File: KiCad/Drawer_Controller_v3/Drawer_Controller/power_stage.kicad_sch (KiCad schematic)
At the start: 27 parts, among them U10 AMS1117-3.3, U9 TPS54331DR

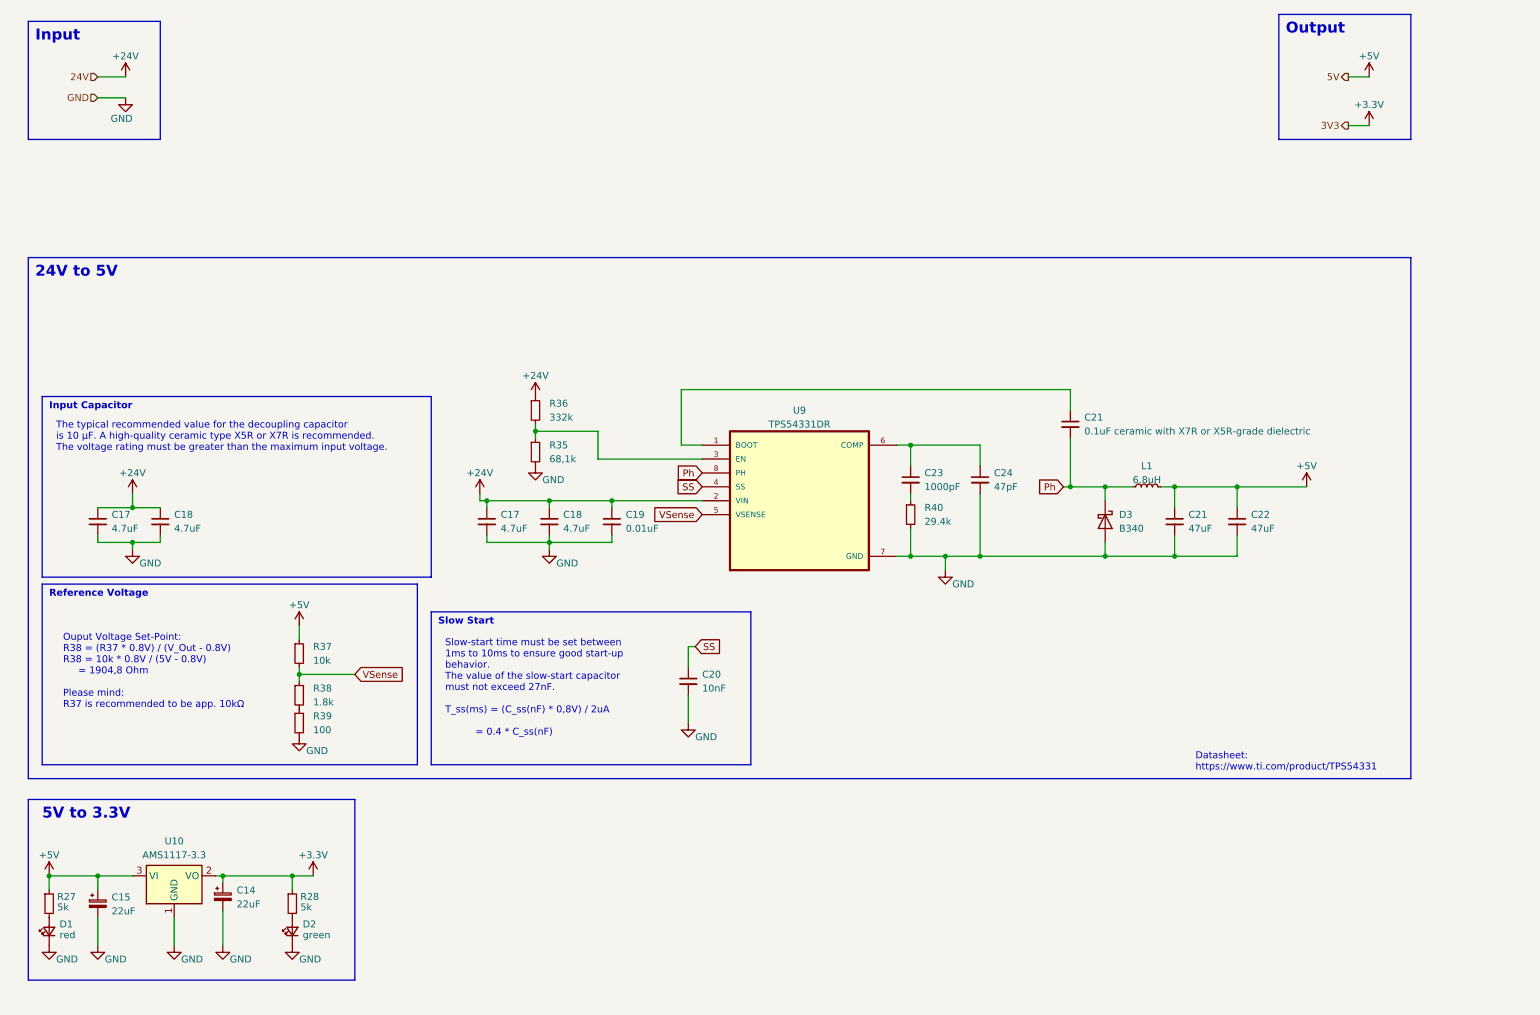
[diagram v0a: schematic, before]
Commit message: Further progress with the power stage including lots of documentation
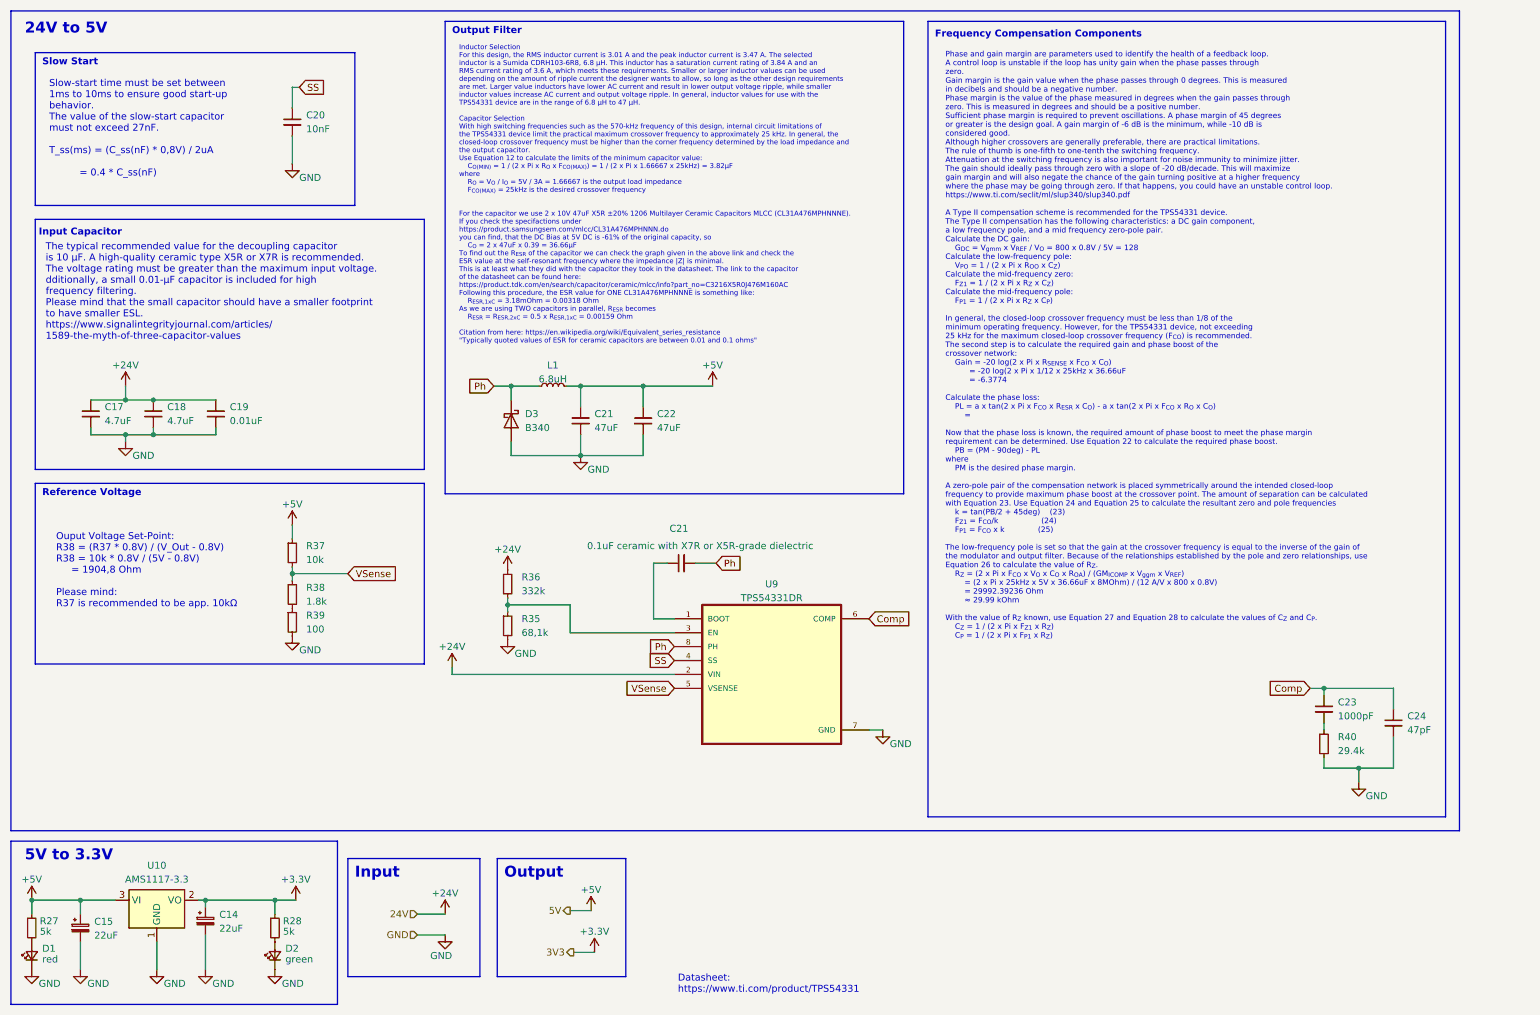
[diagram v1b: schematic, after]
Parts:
- removed C17 (x2), C18 (x2): 4.7uF, symbol Device:C_Small
- added C17, C18: 4.7uF, symbol Device:C_Small
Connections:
- net +24V: now also C17.1, C18.1
- net GND: now also C17.2, C18.2
- net Comp: now reaches C23.1, C24.1, U9.6 (COMP)
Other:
- note added: "Frequency Compensation Components"
- note added: "Inductor Selection For this design, the RMS inductor current is 3.01 A and the peak inductor current is 3.47 A. The selected inductor is a Sumida CDRH103-6R8, 6.8 μH. This inductor has a saturation current rating of 3.84 A and an RMS current rating of 3.6 A, which meets these requirements. Smaller or larger inductor values can be used depending on the amount of ripple current the designer wants t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"
- note added: "Output Filter"
- note added: "Phase and gain margin are parameters used to identify the health of a feedback loop. A control loop is unstable if the loop has unity gain when the phase passes through zero. Gain margin is the gain value when the phase passes through 0 degrees. This is measured in decibels and should be a negative number. Phase margin is the value of the phase measured in degrees when the gain passes through zer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"
- note added: "The typical recommended value for the decoupling capacitor is 10 μF. A high-quality ceramic type X5R or X7R is recommended. The voltage rating must be greater than the maximum input voltage. dditionally, a small 0.01-μF capacitor is included for high frequency filtering. Please mind that the small capacitor should have a smaller footprint to have smaller ESL. https://www.signalintegrityjournal.co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"
- note removed: "The typical recommended value for the decoupling capacitor is 10 μF. A high-quality ceramic type X5R or X7R is recommended. The voltage rating must be greater than the maximum input voltage."
- moved on the sheet: C14, C15, C20, C21, C22, D1, D2, D3, L1, R27, R28, R35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

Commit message: Finished Power Stage
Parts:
- removed C20: 10nF, symbol Device:C_Small
- removed C21: 0.1uF ceramic with X7R or X5R-grade dielectric, symbol Device:C_Small
- removed C23: 1000pF, symbol Device:C_Small
- removed C24: 47pF, symbol Device:C_Small
- removed D3: B340, Diode_SMD:D_SMC, symbol Diode:B340
- removed R35: 68,1k, symbol Device:R_Small
- removed R36: 332k, symbol Device:R_Small
- removed R39: 100, symbol Device:R_Small
- removed R40: 29.4k, symbol Device:R_Small
- removed U9: TPS54331DR, SOIC127P599X175-8N, symbol TPS54331DR:TPS54331DR
- added C17: 4.7uF, symbol Device:C_Small
- added C21: 100nF, symbol Device:C_Small
- added C21: 1uF, symbol Device:C_Small
- added C22 (x2): 22uF, symbol Device:C_Small
- added R37: 100k, symbol Device:R_Small
- added U11: LMR33630ADDAR, VREG_LM5017MR/NOPB, symbol LMR33630ADDAR:LMR33630ADDAR
- C19: value 0.01uF -> 220nF
- C21, C22: value 47uF -> 22uF
- L1: value 6.8uH -> 15uH
- R37: value 10k -> 100k
- R38: value 1.8k -> 24.9k
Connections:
- net +24V: now also C17.1, U11.2 (VIN), U11.3 (EN)
- net +5V: now also C22.1, C22.1
- net GND: now also R38.2, C17.2, C21.2, C22.2, C22.2, U11.1 (PGND), U11.9 (AGND)
- net Ph renamed SW
- net SW: now also C21.2, U11.8 (SW)
- net VSense renamed FB
- net FB: now also U11.5 (FB)
- new net: R37.2, U11.4 (PG)
- new net: C21.1, R37.1, U11.6 (VCC)
- new net: C21.1, U11.7 (BOOT)
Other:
- note added: "A high-quality ceramic capacitor of 100 nF and at least 10 V is required"
- note added: "A minimum of 10 μF of ceramic capacitance is required on the input of the LMR33630. This must be rated for at least the maximum input voltage that the application requires; preferably twice the maximum input voltage. This capacitance can be increased to help reduce input voltage ripple and maintain the input voltage during load transients. In addition, a small case size, 220-nF ceramic capacitor 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"
- note added: "Inductor Selection The parameters for selecting the inductor are the inductance and saturation current. The inductance is based on the desired peak-to-peak ripple current and is normally chosen to be in the range of 20% to 40% of the maximum output current. Experience shows that the best value for inductor ripple current is 30% of the maximum load current. Note that when selecting the ripple curr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"
- note added: "Ouput Voltage Set-Point: R38 = R37 / (V_Out/1V) - 1) R38 = 100k / (5V - 1V) = 25k Please mind: R37 is recommended to be app. 100kΩ For R38 = 24.9k is chosen as recommended in the datasheet"
- note removed: "Frequency Compensation Components"
- note removed: "Inductor Selection For this design, the RMS inductor current is 3.01 A and the peak inductor current is 3.47 A. The selected inductor is a Sumida CDRH103-6R8, 6.8 μH. This inductor has a saturation current rating of 3.84 A and an RMS current rating of 3.6 A, which meets these requirements. Smaller or larger inductor values can be used depending on the amount of ripple current the designer wants t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"
- note removed: "Ouput Voltage Set-Point: R38 = (R37 * 0.8V) / (V_Out - 0.8V) R38 = 10k * 0.8V / (5V - 0.8V) = 1904,8 Ohm Please mind: R37 is recommended to be app. 10kΩ"
- note removed: "Phase and gain margin are parameters used to identify the health of a feedback loop. A control loop is unstable if the loop has unity gain when the phase passes through zero. Gain margin is the gain value when the phase passes through 0 degrees. This is measured in decibels and should be a negative number. Phase margin is the value of the phase measured in degrees when the gain passes through zer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"
- note removed: "Slow Start"
- note removed: "Slow-start time must be set between 1ms to 10ms to ensure good start-up behavior. The value of the slow-start capacitor must not exceed 27nF. T_ss(ms) = (C_ss(nF) * 0,8V) / 2uA = 0.4 * C_ss(nF)"
- note removed: "The typical recommended value for the decoupling capacitor is 10 μF. A high-quality ceramic type X5R or X7R is recommended. The voltage rating must be greater than the maximum input voltage. dditionally, a small 0.01-μF capacitor is included for high frequency filtering. Please mind that the small capacitor should have a smaller footprint to have smaller ESL. https://www.signalintegrityjournal.co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"
- moved on the sheet: C14, C15, C17, C18, C19, C21, C22, D1, D2, L1, R27, R28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

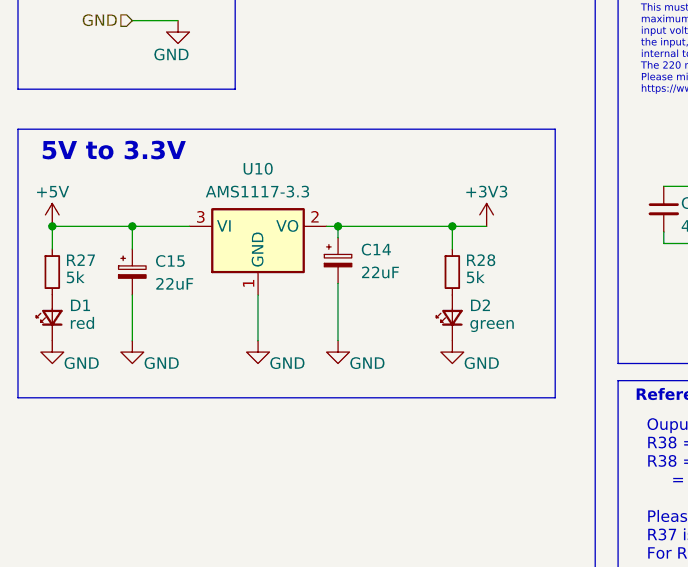
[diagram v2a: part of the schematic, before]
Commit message: Finished ESP32 schematic
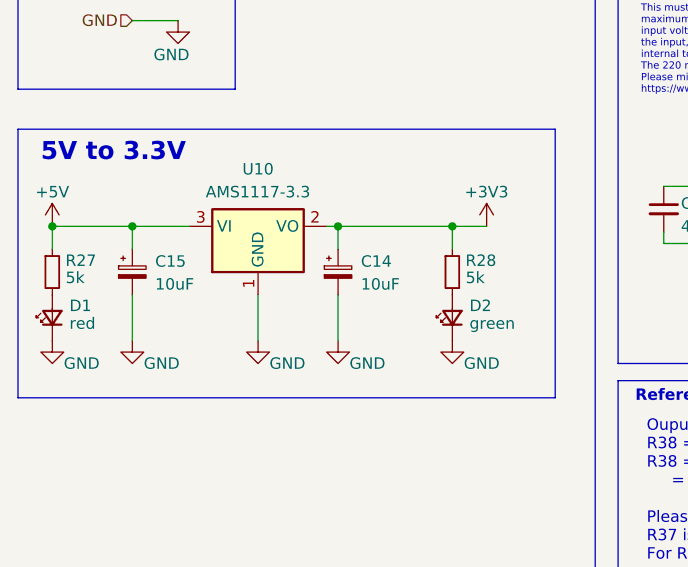
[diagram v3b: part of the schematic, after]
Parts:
- C14, C15: value 22uF -> 10uF
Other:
- moved on the sheet: C14
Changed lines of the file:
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@@
     (stroke (width 0) (type default))
   )
-  (wire (pts (xy 50.8 52.07) (xy 50.8 53.34))
+  (wire (pts (xy 50.8 52.07) (xy 50.8 54.61))
     (stroke (width 0) (type default))
   )
@@
     (stroke (width 0) (type default))
   )
-  (wire (pts (xy 50.8 58.42) (xy 50.8 64.77))
+  (wire (pts (xy 50.8 59.69) (xy 50.8 64.77))
     (stroke (width 0) (type default))
   )
@@
       (effects (font (size 1.27 1.27)) (justify left))
     )
-    (property "Value" "22uF" (at 30.48 58.5089 0)
+    (property "Value" "10uF" (at 30.48 58.5089 0)
       (effects (font (size 1.27 1.27)) (justify left))
     )
@@
     )
   )
-  (symbol (lib_id "Device:C_Polarized_Small") (at 50.8 55.88 0) (unit 1)
+  (symbol (lib_id "Device:C_Polarized_Small") (at 50.8 57.15 0) (unit 1)
     (in_bom yes) (on_board yes) (dnp no) (fields_autoplaced)
-    (property "Reference" "C14" (at 53.34 54.6989 0)
-      (effects (font (size 1.27 1.27)) (justify left))
-    )
-    (property "Value" "22uF" (at 53.34 57.2389 0)
-      (effects (font (size 1.27 1.27)) (justify left))
-    )
-    (property "Footprint" "" (at 50.8 55.88 0)
-      (effects (font (size 1.27 1.27)) hide)
-    )
-    (property "Datasheet" "~" (at 50.8 55.88 0)
-      (effects (font (size 1.27 1.27)) hide)
-    )
+    (property "Reference" "C14" (at 53.34 55.9689 0)
+      (effects (font (size 1.27 1.27)) (justify left))
+    )
+    (property "Value" "10uF" (at 53.34 58.5089 0)
+      (effects (font (size 1.27 1.27)) (justify left))
+    )
+    (property "Footprint" "" (at 50.8 57.15 0)
+      (effects (font (size 1.27 1.27)) hide)
+    )
+    (property "Datasheet" "~" (at 50.8 57.15 0)
+      (effects (font (size 1.27 1.27)) hide)
+    )

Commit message: Finished schematic for electrical drawer
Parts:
- D2: value green -> yellow
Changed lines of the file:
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@@
   (symbol (lib_id "power:+3V3") (at 67.31 52.07 0) (unit 1)
     (in_bom yes) (on_board yes) (dnp no) (fields_autoplaced)
-    (property "Reference" "#PWR060" (at 67.31 55.88 0)
+    (property "Reference" "#PWR065" (at 67.31 55.88 0)
       (effects (font (size 1.27 1.27)) hide)
     )
@@
   (symbol (lib_id "power:+3V3") (at 273.685 33.02 0) (unit 1)
     (in_bom yes) (on_board yes) (dnp no) (fields_autoplaced)
-    (property "Reference" "#PWR065" (at 273.685 36.83 0)
+    (property "Reference" "#PWR078" (at 273.685 36.83 0)
       (effects (font (size 1.27 1.27)) hide)
     )
@@
   (symbol (lib_name "+5V_1") (lib_id "power:+5V") (at 193.675 76.835 0) (unit 1)
     (in_bom yes) (on_board yes) (dnp no) (fields_autoplaced)
-    (property "Reference" "#PWR066" (at 193.675 80.645 0)
+    (property "Reference" "#PWR073" (at 193.675 80.645 0)
       (effects (font (size 1.27 1.27)) hide)
     )
@@
       (effects (font (size 1.27 1.27)) (justify right))
     )
-    (property "Value" "green" (at 65.405 62.865 90)
+    (property "Value" "yellow" (at 65.405 62.865 90)
       (effects (font (size 1.27 1.27)) (justify right))
     )
@@
   (symbol (lib_name "+5V_1") (lib_id "power:+5V") (at 273.05 25.4 0) (unit 1)
     (in_bom yes) (on_board yes) (dnp no) (fields_autoplaced)
-    (property "Reference" "#PWR069" (at 273.05 29.21 0)
-      (effects (font (size 1.27 1.27)) hide)
-    )
+    (property "Reference" "#PWR077" (at 273.05 29.21 0)
+      (effects (font (size 1.27 1.27)) hide)
+    )
